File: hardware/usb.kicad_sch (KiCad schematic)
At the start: 11 parts, among them J8 USB-C, SW1 RESET, U3 USBLC6-2SC6, Y1 8MHz CL=20pF

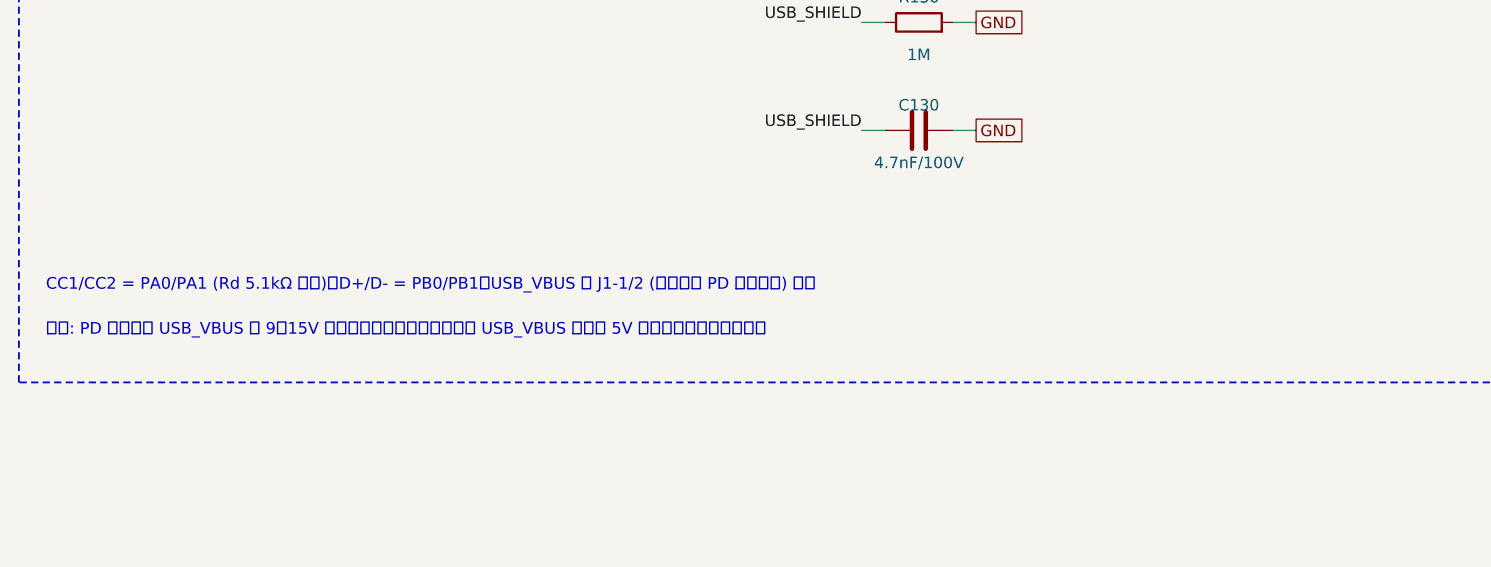
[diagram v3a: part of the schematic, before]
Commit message: Rev 0.4: rework module pinout for routability, power boards regenerated
- Module edge pin order follows the CH32M030 QFN48 pin sides so the
  breakout traces nest instead of crossing (J1: USB_VBUS, PD_PWR_EN,
  PC4/PC5, +3V3, +5V, SWDIO, VBUS, NTC, BEMF, HALL, ISx, TACH;
  J2: RX/TX, nRST, gate drive HO3..LO0, VBUS_SNS, I2C, nFAULT).
- Module: area under the QFN kept for fan-out (filters and the VHV/USB
  diode block moved away, gate LEDs right-aligned to J2).
- Power boards A/B/C re-placed for the new pinout (VBUS divider next to
  J2 VBUS_SNS, LM74700 next to its FET) and re-routed: all three at
  0 unconnected / 0 electrical DRC errors.
- Layout tooling: DRC via kicad-cli in a separate process, reload after
  SES import, selectable Freerouting jar, optional rip-up repair,
  configurable Freerouting timeout.
- MCU module still has unrouted connections (work in progress).

Co-Authored-By: Claude Opus 5.5 <noreply@anthropic.com>
Claude-Session: https://claude.ai/code/session_01LENFjjhDfYjJZV1NWhB9uV
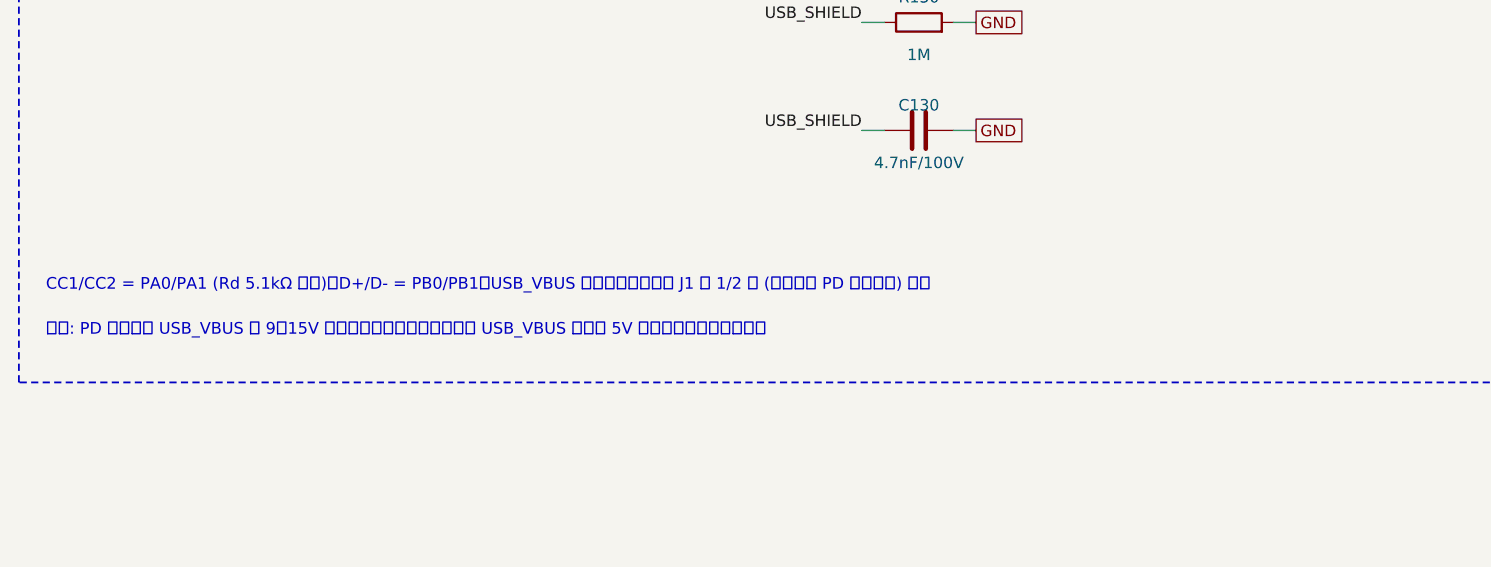
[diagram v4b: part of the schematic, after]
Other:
- note added: "CC1/CC2 = PA0/PA1 (Rd 5.1kΩ 内蔵)。D+/D- = PB0/PB1。USB_VBUS はモジュール端子 J1 の 1/2 番 (子基板の PD 給電経路) へ。"
- note removed: "CC1/CC2 = PA0/PA1 (Rd 5.1kΩ 内蔵)。D+/D- = PB0/PB1。USB_VBUS は J1-1/2 (子基板の PD 給電経路) へ。"
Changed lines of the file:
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@@
 (rectangle (start 260 110) (end 405 190) (stroke (width 0.2) (type dash)) (fill (type none)))
 (text "リセット (RST = PC0)  ※ 上面" (exclude_from_sim no) (at 262 115 0) (effects (font (size 2 2) (thickness 0.3) (bold yes)) (justify left bottom)))
-(text "CC1/CC2 = PA0/PA1 (Rd 5.1kΩ 内蔵)。D+/D- = PB0/PB1。USB_VBUS は J1-1/2 (子基板の PD 給電経路) へ。" (exclude_from_sim no) (at 23 140 0) (effects (font (size 1.3 1.3)) (justify left bottom)))
+(text "CC1/CC2 = PA0/PA1 (Rd 5.1kΩ 内蔵)。D+/D- = PB0/PB1。USB_VBUS はモジュール端子 J1 の 1/2 番 (子基板の PD 給電経路) へ。" (exclude_from_sim no) (at 23 140 0) (effects (font (size 1.3 1.3)) (justify left bottom)))
 (text "注意: PD 契約後は USB_VBUS が 9〜15V になる。ブレッドボードでは USB_VBUS ピンに 5V 部品を直結しないこと。" (exclude_from_sim no) (at 23 145 0) (effects (font (size 1.3 1.3)) (justify left bottom)))
 (text "XI=PB5 / XO=PB6。C = 2 x (CL - 浮遊容量 約5pF) = 30pF。" (exclude_from_sim no) (at 263 92 0) (effects (font (size 1.3 1.3)) (justify left bottom)))
